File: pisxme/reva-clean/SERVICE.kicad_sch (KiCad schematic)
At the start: 0 parts

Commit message: add native Phase 3 contract connectivity
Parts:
- added X: SERVICE_Contract
- added XSE: SERVICE_Contract, symbol PiSXMeRevAClean:SERVICE_Contract
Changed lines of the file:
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@@
 (kicad_sch (version 20230409) (generator "eeschema")
   (paper "A4")
+    (symbol "PiSXMeRevAClean:SERVICE_Contract"
+      (pin_names (offset 1.0))
+      (exclude_from_sim no)
+      (in_bom yes)
+      (on_board yes)
+      (property "Reference" "X"
+        (at 0 -7.039999999999999 0)
+        (effects (font (size 1.27 1.27))))
+      (property "Value" "SERVICE_Contract"
+        (at 0 7.039999999999999 0)
+        (effects (font (size 1.27 1.27))))
+      (property "Footprint" ""
+        (at 0 0 0)
+        (effects (font (size 1.27 1.27)) (hide yes)))
+      (property "Datasheet" "~"
+        (at 0 0 0)
+        (effects (font (size 1.27 1.27)) (hide yes)))
+      (symbol "SERVICE_Contract_1_1"
+        (rectangle (start -1.27 -5.77) (end 1.27 5.77)
+          (stroke (width 0.254) (type default)) (fill (type background)))
+        (pin passive line
+          (at -5.08 0 0)
+          (length 3.81)
+          (name "SERVICE_USB2" (effects (font (size 1.27 1.27))))
+          (number "1" (effects (font (size 1.27 1.27)))))
+        (pin passive line
+          (at -5.08 3 0)
+          (length 3.81)
+          (name "SERVICE_VBUS_SENSE" (effects (font (size 1.27 1.27))))
+          (number "2" (effects (font (size 1.27 1.27)))))
+        (pin passive line
+          (at -5.08 6 0)
+          (length 3.81)
+          (name "SERVICE_RD" (effects (font (size 1.27 1.27))))
+          (number "3" (effects (font (size 1.27 1.27)))))
+        (pin passive line
+          (at -5.08 9 0)
+          (length 3.81)
+          (name "SERVICE_GND" (effects (font (size 1.27 1.27))))
+          (number "4" (effects (font (size 1.27 1.27)))))
+      )
+    )
   (hierarchical_label "SERVICE_USB2"
     (shape bidirectional)
@@
     (effects (font (size 1.27 1.27)) (justify left))
 )
-  (sheet_instances (path "/8" (page "8")))
+  (wire
+    (pts (xy 5 10) (xy 19.92 10))
+    (stroke (width 0) (type default))
 )
+  (wire
+    (pts (xy 5 13) (xy 19.92 13))
+    (stroke (width 0) (type default))
+)
+  (wire
+    (pts (xy 5 16) (xy 19.92 16))
+    (stroke (width 0) (type default))
+)
+  (wire
+    (pts (xy 5 19) (xy 19.92 19))
+    (stroke (width 0) (type default))
+)
+  (symbol
+    (lib_id "PiSXMeRevAClean:SERVICE_Contract")
+    (at 25 10 0)
+    (unit 1)
+    (exclude_from_sim no)
+    (in_bom no)
+    (on_board no)
+    (dnp no)
+    (property "Reference" "XSE"
+      (at 25 5 0)
+      (effects (font (size 1.27 1.27))))
+    (property "Value" "SERVICE_Contract"
+      (at 25 18 0)
+      (effects (font (size 1.27 1.27))))
+    (property "Footprint" ""
+      (at 25 10 0)
+      (effects (font (size 1.27 1.27)) (hide yes)))
+    (property "Datasheet" "~"
+      (at 25 10 0)
+      (effects (font (size 1.27 1.27)) (hide yes)))
+    (pin "1")
+    (pin "2")
+    (pin "3")
+    (pin "4")
+    (instances (project "PiSXMe_RevA_Clean"
+      (path "/30000000-0000-0000-0000-000000000000/10000000-0000-0000-0000-000000000008" (reference "XSE" ) (unit 1))))
+  )
+  (sheet_instances (path "/30000000-0000-0000-0000-000000000000/10000000-0000-0000-0000-000000000008" (page "8")))
+)

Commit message: close native Phase 3 hierarchy association
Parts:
- removed X: SERVICE_Contract
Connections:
- net SERVICE_GND: now also XSE.4 (SERVICE_GND)
- net SERVICE_RD: now also XSE.3 (SERVICE_RD)
- net SERVICE_USB2: now also XSE.1 (SERVICE_USB2)
- net SERVICE_VBUS_SENSE: now also XSE.2 (SERVICE_VBUS_SENSE)
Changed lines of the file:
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@@
 (kicad_sch (version 20230409) (generator "eeschema")
   (paper "A4")
-    (symbol "PiSXMeRevAClean:SERVICE_Contract"
-      (pin_names (offset 1.0))
-      (exclude_from_sim no)
-      (in_bom yes)
-      (on_board yes)
-      (property "Reference" "X"
-        (at 0 -7.039999999999999 0)
-        (effects (font (size 1.27 1.27))))
-      (property "Value" "SERVICE_Contract"
-        (at 0 7.039999999999999 0)
-        (effects (font (size 1.27 1.27))))
-      (property "Footprint" ""
-        (at 0 0 0)
-        (effects (font (size 1.27 1.27)) (hide yes)))
-      (property "Datasheet" "~"
-        (at 0 0 0)
-        (effects (font (size 1.27 1.27)) (hide yes)))
-      (symbol "SERVICE_Contract_1_1"
-        (rectangle (start -1.27 -5.77) (end 1.27 5.77)
-          (stroke (width 0.254) (type default)) (fill (type background)))
-        (pin passive line
-          (at -5.08 0 0)
-          (length 3.81)
-          (name "SERVICE_USB2" (effects (font (size 1.27 1.27))))
-          (number "1" (effects (font (size 1.27 1.27)))))
-        (pin passive line
-          (at -5.08 3 0)
-          (length 3.81)
-          (name "SERVICE_VBUS_SENSE" (effects (font (size 1.27 1.27))))
-          (number "2" (effects (font (size 1.27 1.27)))))
-        (pin passive line
-          (at -5.08 6 0)
-          (length 3.81)
-          (name "SERVICE_RD" (effects (font (size 1.27 1.27))))
-          (number "3" (effects (font (size 1.27 1.27)))))
-        (pin passive line
-          (at -5.08 9 0)
-          (length 3.81)
-          (name "SERVICE_GND" (effects (font (size 1.27 1.27))))
-          (number "4" (effects (font (size 1.27 1.27)))))
-      )
-    )
   (hierarchical_label "SERVICE_USB2"
     (shape bidirectional)
-    (at 5 10 0)
-    (effects (font (size 1.27 1.27)) (justify left))
+    (at 5 10 180)
+    (effects (font (size 1.27 1.27)) (justify right))
 )
   (hierarchical_label "SERVICE_VBUS_SENSE"
     (shape bidirectional)
-    (at 5 13 0)
-    (effects (font (size 1.27 1.27)) (justify left))
+    (at 5 13 180)
+    (effects (font (size 1.27 1.27)) (justify right))
 )
   (hierarchical_label "SERVICE_RD"
     (shape bidirectional)
-    (at 5 16 0)
-    (effects (font (size 1.27 1.27)) (justify left))
+    (at 5 16 180)
+    (effects (font (size 1.27 1.27)) (justify right))
 )
   (hierarchical_label "SERVICE_GND"
     (shape bidirectional)
-    (at 5 19 0)
-    (effects (font (size 1.27 1.27)) (justify left))
+    (at 5 19 180)
+    (effects (font (size 1.27 1.27)) (justify right))
 )
   (wire

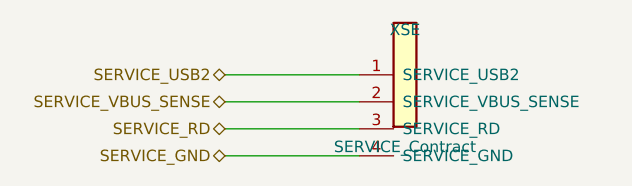
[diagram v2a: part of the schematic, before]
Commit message: stabilize Phase 3 hierarchy netlist references
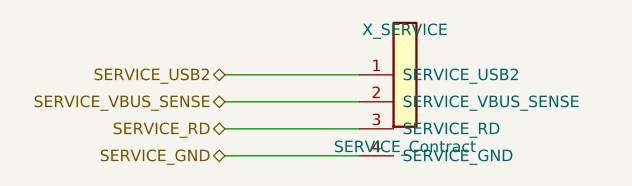
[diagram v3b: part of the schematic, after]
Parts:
- renumbered XSE to X_SERVICE
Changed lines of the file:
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@@
     (on_board no)
     (dnp no)
-    (property "Reference" "XSE"
+    (property "Reference" "X_SERVICE"
       (at 25 5 0)
       (effects (font (size 1.27 1.27))))
@@
     (pin "4")
     (instances (project "PiSXMe_RevA_Clean"
-      (path "/30000000-0000-0000-0000-000000000000/10000000-0000-0000-0000-000000000008" (reference "XSE" ) (unit 1))))
+      (path "/30000000-0000-0000-0000-000000000000/10000000-0000-0000-0000-000000000008" (reference "X_SERVICE" ) (unit 1))))
   )
   (sheet_instances (path "/30000000-0000-0000-0000-000000000000/10000000-0000-0000-0000-000000000008" (page "8")))

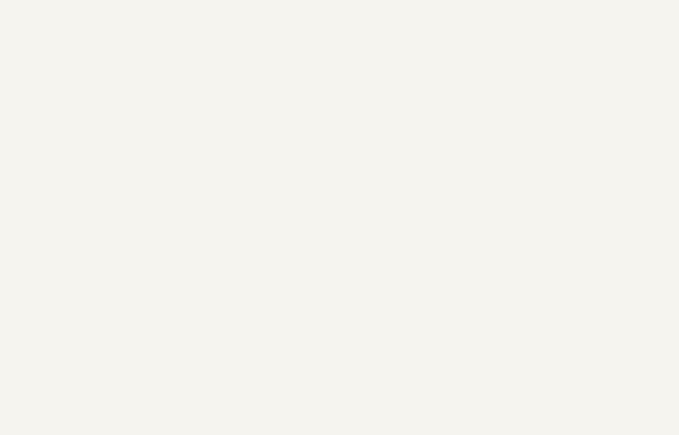
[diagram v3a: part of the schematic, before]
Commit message: close Phase 8 SERVICE island
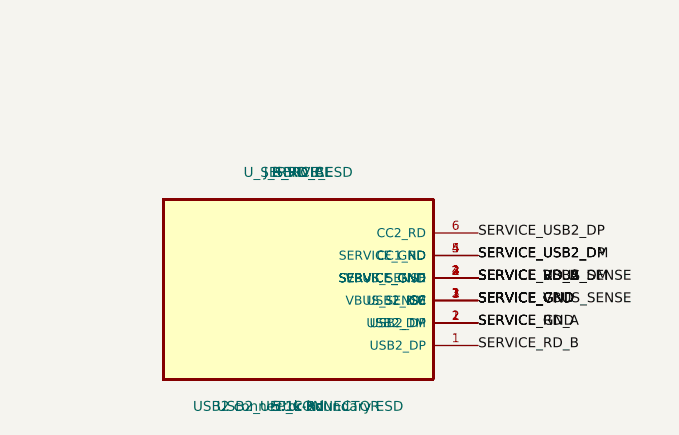
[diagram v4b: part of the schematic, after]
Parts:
- added J_SERVICE: USB2_UFP_CONNECTOR, symbol PiSXMeRevAClean:USB2_UFP_CONNECTOR
- added R_RD_A, R_RD_B: 5.1k Rd, symbol PiSXMeRevAClean:USB2_RD_5K1
- added U_SERVICE_ESD: USB2 connector-boundary ESD, symbol PiSXMeRevAClean:USB2_ESD
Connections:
- net SERVICE_VBUS_SENSE is gone; now on net SERVICE_GND: X_SERVICE.2 (SERVICE_VBUS_SENSE)
- net SERVICE_GND: now also J_SERVICE.1 (USB2_DP), J_SERVICE.2 (USB2_DM), J_SERVICE.3 (VBUS_SENSE), J_SERVICE.4 (SERVICE_GND), J_SERVICE.5 (CC1_RD), J_SERVICE.6 (CC2_RD), R_RD_A.1 (CC), R_RD_A.2 (SERVICE_GND), R_RD_B.1 (CC), R_RD_B.2 (SERVICE_GND), U_SERVICE_ESD.1 (USB2_DP), U_SERVICE_ESD.2 (USB2_DM), U_SERVICE_ESD.3 (VBUS_SENSE), U_SERVICE_ESD.4 (SERVICE_GND)
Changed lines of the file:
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@@
       (path "/30000000-0000-0000-0000-000000000000/10000000-0000-0000-0000-000000000008" (reference "X_SERVICE" ) (unit 1))))
   )
+(label "SERVICE_USB2_DP" (at 70 88.75 0) (effects (font (size 1.1 1.1)) (justify left)))
+(label "SERVICE_USB2_DM" (at 70 91.25 0) (effects (font (size 1.1 1.1)) (justify left)))
+(label "SERVICE_VBUS_SENSE" (at 70 93.75 0) (effects (font (size 1.1 1.1)) (justify left)))
+(label "SERVICE_GND" (at 70 96.25 0) (effects (font (size 1.1 1.1)) (justify left)))
+(label "SERVICE_RD_A" (at 70 98.75 0) (effects (font (size 1.1 1.1)) (justify left)))
+(label "SERVICE_RD_B" (at 70 101.25 0) (effects (font (size 1.1 1.1)) (justify left)))
+(symbol (lib_id "PiSXMeRevAClean:USB2_UFP_CONNECTOR") (at 50 95 0) (unit 1) (exclude_from_sim no) (in_bom yes) (on_board yes) (dnp no) (property "Reference" "J_SERVICE" (at 50 82 0) (effects (font (size 1.1 1.1)))) (property "Value" "USB2_UFP_CONNECTOR" (at 50 108 0) (effects (font (size 1.1 1.1)))) (property "MPN" "USB2_UFP_CONNECTOR" (at 50 95 0) (effects (font (size 1 1)) (hide yes))) (property "Footprint" "" (at 50 95 0) (effects (font (size 1 1)) (hide yes))) (pin "1")
+(pin "2")
+(pin "3")
+(pin "4")
+(pin "5")
+(pin "6") (instances (project "PiSXMe_RevA_Clean" (path "/30000000-0000-0000-0000-000000000000" (reference "J_SERVICE") (unit 1)))) )(label "SERVICE_USB2_DP" (at 70 91.25 0) (effects (font (size 1.1 1.1)) (justify left)))
+(label "SERVICE_USB2_DM" (at 70 93.75 0) (effects (font (size 1.1 1.1)) (justify left)))
+(label "SERVICE_VBUS_SENSE" (at 70 96.25 0) (effects (font (size 1.1 1.1)) (justify left)))
+(label "SERVICE_GND" (at 70 98.75 0) (effects (font (size 1.1 1.1)) (justify left)))
+(symbol (lib_id "PiSXMeRevAClean:USB2_ESD") (at 50 95 0) (unit 1) (exclude_from_sim no) (in_bom yes) (on_board yes) (dnp no) (property "Reference" "U_SERVICE_ESD" (at 50 82 0) (effects (font (size 1.1 1.1)))) (property "Value" "USB2 connector-boundary ESD" (at 50 108 0) (effects (font (size 1.1 1.1)))) (property "MPN" "USB2 connector-boundary ESD" (at 50 95 0) (effects (font (size 1 1)) (hide yes))) (property "Footprint" "" (at 50 95 0) (effects (font (size 1 1)) (hide yes))) (pin "1")
+(pin "2")
+(pin "3")
+(pin "4") (instances (project "PiSXMe_RevA_Clean" (path "/30000000-0000-0000-0000-000000000000" (reference "U_SERVICE_ESD") (unit 1)))) )(label "SERVICE_RD_A" (at 70 93.75 0) (effects (font (size 1.1 1.1)) (justify left)))
+(label "SERVICE_GND" (at 70 96.25 0) (effects (font (size 1.1 1.1)) (justify left)))
+(symbol (lib_id "PiSXMeRevAClean:USB2_RD_5K1") (at 50 95 0) (unit 1) (exclude_from_sim no) (in_bom yes) (on_board yes) (dnp no) (property "Reference" "R_RD_A" (at 50 82 0) (effects (font (size 1.1 1.1)))) (property "Value" "5.1k Rd" (at 50 108 0) (effects (font (size 1.1 1.1)))) (property "MPN" "5.1k Rd" (at 50 95 0) (effects (font (size 1 1)) (hide yes))) (property "Footprint" "" (at 50 95 0) (effects (font (size 1 1)) (hide yes))) (pin "1")
+(pin "2") (instances (project "PiSXMe_RevA_Clean" (path "/30000000-0000-0000-0000-000000000000" (reference "R_RD_A") (unit 1)))) )(label "SERVICE_RD_B" (at 70 93.75 0) (effects (font (size 1.1 1.1)) (justify left)))
+(label "SERVICE_GND" (at 70 96.25 0) (effects (font (size 1.1 1.1)) (justify left)))
+(symbol (lib_id "PiSXMeRevAClean:USB2_RD_5K1") (at 50 95 0) (unit 1) (exclude_from_sim no) (in_bom yes) (on_board yes) (dnp no) (property "Reference" "R_RD_B" (at 50 82 0) (effects (font (size 1.1 1.1)))) (property "Value" "5.1k Rd" (at 50 108 0) (effects (font (size 1.1 1.1)))) (property "MPN" "5.1k Rd" (at 50 95 0) (effects (font (size 1 1)) (hide yes))) (property "Footprint" "" (at 50 95 0) (effects (font (size 1 1)) (hide yes))) (pin "1")
+(pin "2") (instances (project "PiSXMe_RevA_Clean" (path "/30000000-0000-0000-0000-000000000000" (reference "R_RD_B") (unit 1)))) )
   (sheet_instances (path "/30000000-0000-0000-0000-000000000000/10000000-0000-0000-0000-000000000008" (page "8")))
 )

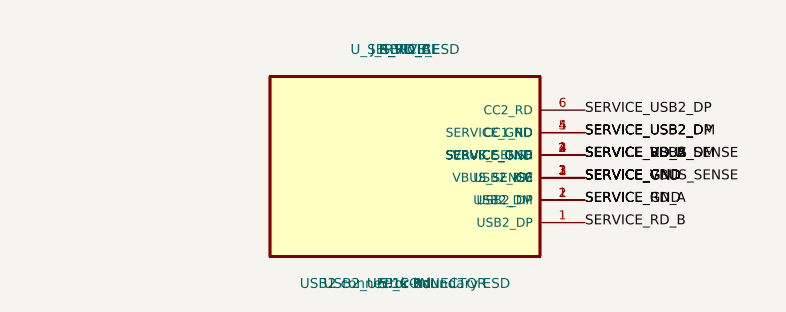
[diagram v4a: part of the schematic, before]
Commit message: close USB-C service footprint authority
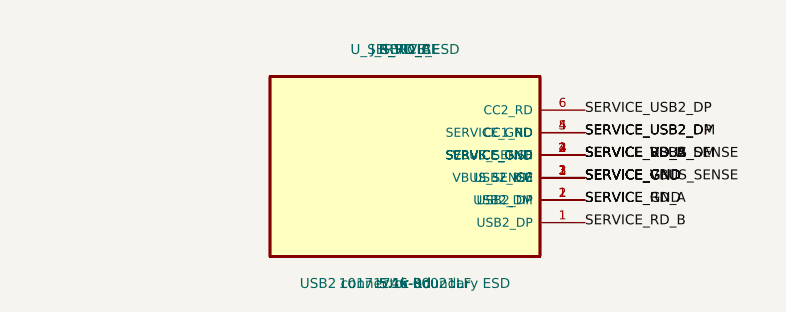
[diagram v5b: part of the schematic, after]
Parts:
- J_SERVICE: value USB2_UFP_CONNECTOR -> 10171746-00021LF; footprint (none) -> PiSXMeRevAClean:USB_C_SERVICE_10171746; MPN USB2_UFP_CONNECTOR -> 10171746-00021LF
- U_SERVICE_ESD: footprint (none) -> PiSXMeRevAClean:USB_C_SERVICE_10171746
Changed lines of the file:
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@@
 (label "SERVICE_RD_A" (at 70 98.75 0) (effects (font (size 1.1 1.1)) (justify left)))
 (label "SERVICE_RD_B" (at 70 101.25 0) (effects (font (size 1.1 1.1)) (justify left)))
-(symbol (lib_id "PiSXMeRevAClean:USB2_UFP_CONNECTOR") (at 50 95 0) (unit 1) (exclude_from_sim no) (in_bom yes) (on_board yes) (dnp no) (property "Reference" "J_SERVICE" (at 50 82 0) (effects (font (size 1.1 1.1)))) (property "Value" "USB2_UFP_CONNECTOR" (at 50 108 0) (effects (font (size 1.1 1.1)))) (property "MPN" "USB2_UFP_CONNECTOR" (at 50 95 0) (effects (font (size 1 1)) (hide yes))) (property "Footprint" "" (at 50 95 0) (effects (font (size 1 1)) (hide yes))) (pin "1")
+(symbol (lib_id "PiSXMeRevAClean:USB2_UFP_CONNECTOR") (at 50 95 0) (unit 1) (exclude_from_sim no) (in_bom yes) (on_board yes) (dnp no) (property "Reference" "J_SERVICE" (at 50 82 0) (effects (font (size 1.1 1.1)))) (property "Value" "10171746-00021LF" (at 50 108 0) (effects (font (size 1.1 1.1)))) (property "MPN" "10171746-00021LF" (at 50 95 0) (effects (font (size 1 1)) (hide yes))) (property "Footprint" "PiSXMeRevAClean:USB_C_SERVICE_10171746" (at 50 95 0) (effects (font (size 1 1)) (hide yes))) (pin "1")
 (pin "2")
 (pin "3")
@@
 (label "SERVICE_VBUS_SENSE" (at 70 96.25 0) (effects (font (size 1.1 1.1)) (justify left)))
 (label "SERVICE_GND" (at 70 98.75 0) (effects (font (size 1.1 1.1)) (justify left)))
-(symbol (lib_id "PiSXMeRevAClean:USB2_ESD") (at 50 95 0) (unit 1) (exclude_from_sim no) (in_bom yes) (on_board yes) (dnp no) (property "Reference" "U_SERVICE_ESD" (at 50 82 0) (effects (font (size 1.1 1.1)))) (property "Value" "USB2 connector-boundary ESD" (at 50 108 0) (effects (font (size 1.1 1.1)))) (property "MPN" "USB2 connector-boundary ESD" (at 50 95 0) (effects (font (size 1 1)) (hide yes))) (property "Footprint" "" (at 50 95 0) (effects (font (size 1 1)) (hide yes))) (pin "1")
+(symbol (lib_id "PiSXMeRevAClean:USB2_ESD") (at 50 95 0) (unit 1) (exclude_from_sim no) (in_bom yes) (on_board yes) (dnp no) (property "Reference" "U_SERVICE_ESD" (at 50 82 0) (effects (font (size 1.1 1.1)))) (property "Value" "USB2 connector-boundary ESD" (at 50 108 0) (effects (font (size 1.1 1.1)))) (property "MPN" "USB2 connector-boundary ESD" (at 50 95 0) (effects (font (size 1 1)) (hide yes))) (property "Footprint" "PiSXMeRevAClean:USB_C_SERVICE_10171746" (at 50 95 0) (effects (font (size 1 1)) (hide yes))) (pin "1")
 (pin "2")
 (pin "3")
